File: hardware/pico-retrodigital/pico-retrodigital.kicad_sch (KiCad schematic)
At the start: 43 parts, among them J1 Conn_02x05_Top_Bottom, J2 HDMI_A, J4 Conn_01x02_Pin, J5 USB_C_Plug_USB2.0, SW1 SW_Push, U6 74LVC2G17, U7 RP2350B, U8 NCP1117-3.3_SOT223, Y1 ABM8-272-T3

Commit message: PCB fixes
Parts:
- removed J2: HDMI_A, Connector_Video:HDMI_A_Molex_208658-1001_Horizontal, symbol Connector:HDMI_A
- removed U6: 74LVC2G17, Package_TO_SOT_SMD:SOT-23-6, symbol pico-retrodigital:74LVC2G17_SINGLE
- added C16: 0.1u, Capacitor_SMD:C_0603_1608Metric, symbol Device:C
- added J3: Conn_01x14, Connector_FFC-FPC:TE_1-1734839-4_1x14-1MP_P0.5mm_Horizontal, symbol Connector_Generic:Conn_01x14
- added U1, U2: SN74LVC1G17DBVR, pico-retrodigital:SOT-23-5, symbol pico-retrodigital:SN74LVC1G17DBVR
- C14, C15: footprint RP2350_80QFN_minimal:C_0402_1005Metric_small_pads -> Capacitor_SMD:C_0402_1005Metric
- L1: footprint RP2350_80QFN_minimal:L_pol_2016 -> Inductor_SMD:L_0805_2012Metric
- R16, R17, R18: symbol Device:R_Small -> Device:R
- U3: renamed from U7; value RP2350B -> RP2354B; footprint rpi-lib-kicad-rp235x:QFN-80-1EP_10x10mm_P0.4mm_EP3.4x3.4mm_ThermalVias -> Package_DFN_QFN:QFN-80-1EP_10x10mm_P0.4mm_EP3.4x3.4mm_ThermalVias
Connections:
- net CTL_4 is gone; now on net CTL_2: U3.27 (GPIO26)
- net CTL_5 is gone; now on net CTL_3: U3.28 (GPIO27)
- net VBUS is gone; now on net 5V: C12.1, D3.1 (K), U8.3 (VI)
- net +3V3: now also C16.1, U1.5 (VCC)
- net 3V3: now also U2.5 (VCC)
- net AUD_CLK: now also U3.79 (GPIO2), U2.4 (Y)
- net AUD_DAT: now also U3.77 (GPIO0)
- net AUD_WS: now also U3.78 (GPIO1)
- net AUX_A: now also U3.8 (GPIO10)
- net AUX_B: now also U3.9 (GPIO11)
- net CEC_PICO: now also U3.22 (GPIO22), J3.6 (Pin_6)
- net CLK+: now also J3.8 (Pin_8)
- net CLK-: now also J3.7 (Pin_7)
- net CTL_0: now also U3.25 (GPIO24); no longer U3.22 (GPIO22)
- net CTL_1: now also U3.26 (GPIO25); no longer U3.23 (GPIO23)
- net CTL_2: no longer U3.25 (GPIO24)
- net CTL_3: no longer U3.26 (GPIO25)
- net D0+: now also J3.10 (Pin_10)
- net D0-: now also J3.9 (Pin_9)
- net D1+: now also J3.12 (Pin_12)
- net D1-: now also J3.11 (Pin_11)
- net D2+: now also J3.14 (Pin_14)
- net D2-: now also J3.13 (Pin_13)
- net GND: now also C16.2, J3.3 (Pin_3), U1.2 (GND), U2.2 (GND)
- net IN_AUD_CLK: now also U2.1 (A)
- net IN_PCLK: now also U1.1 (A)
- net PCLK: now also U1.4 (Y)
- net SCL: now also U3.21 (GPIO21), J3.5 (Pin_5)
- net SDA: now also U3.20 (GPIO20), J3.4 (Pin_4)
- net at C6.1, D2.1 (K): now also J3.1 (Pin_1)
- net at R2.2: now also J3.2 (Pin_2)
- no-connect marks 1 -> 21
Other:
- note added: "HDMI FFC"
- moved on the sheet: C6, D2, R1, R17, R18, R2

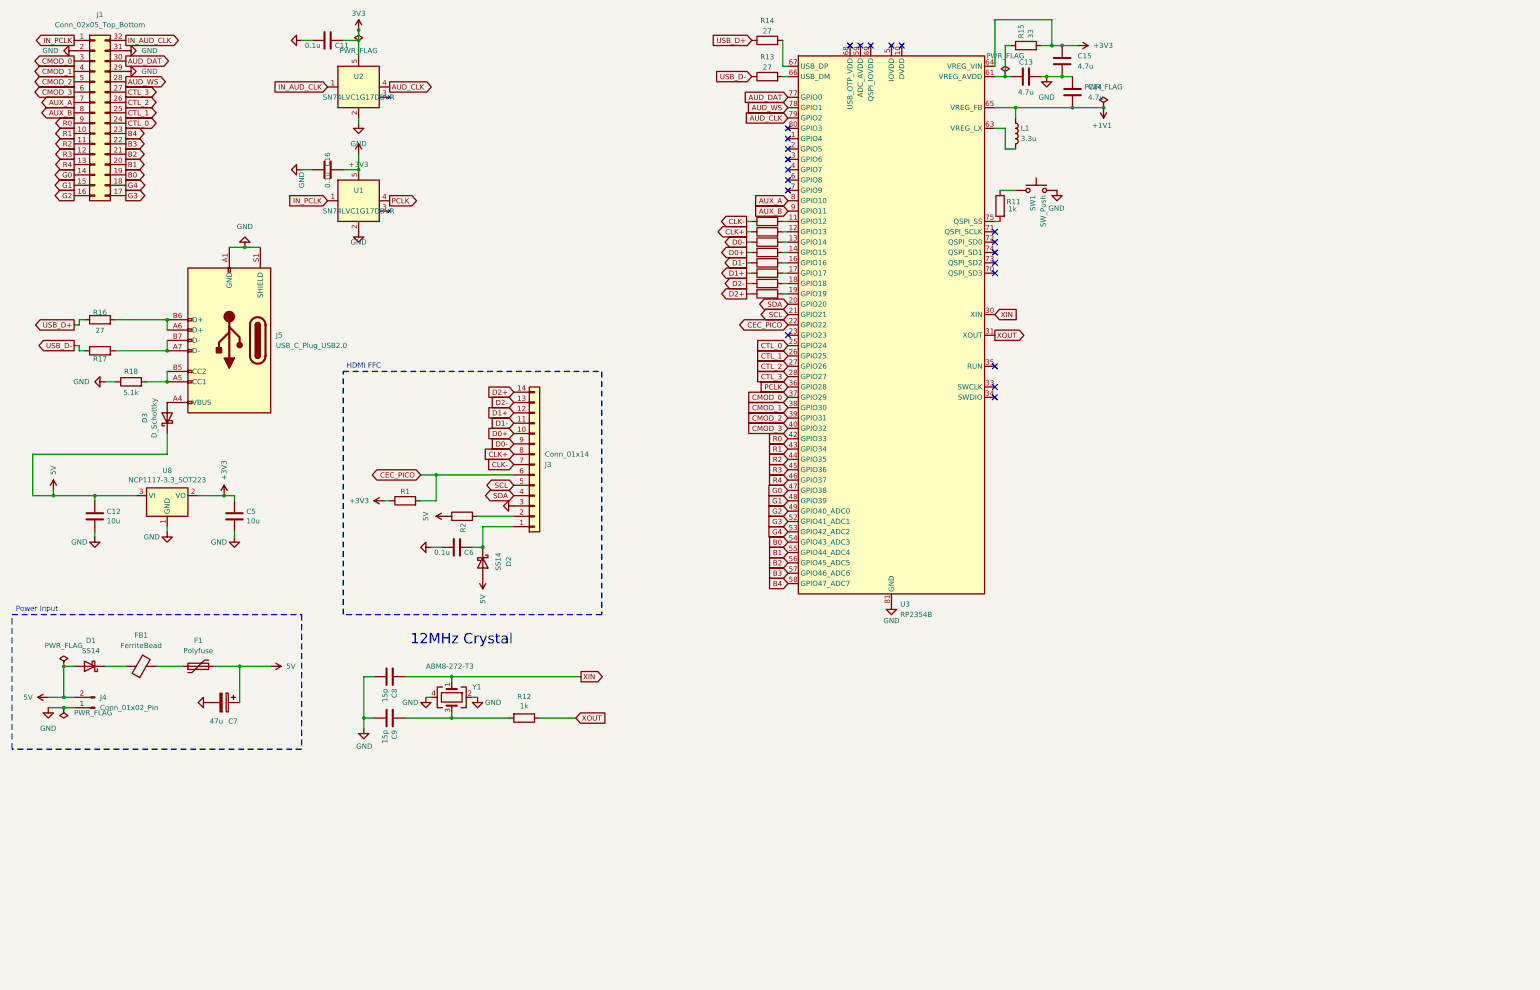
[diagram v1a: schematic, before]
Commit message: Square-shaped PCB
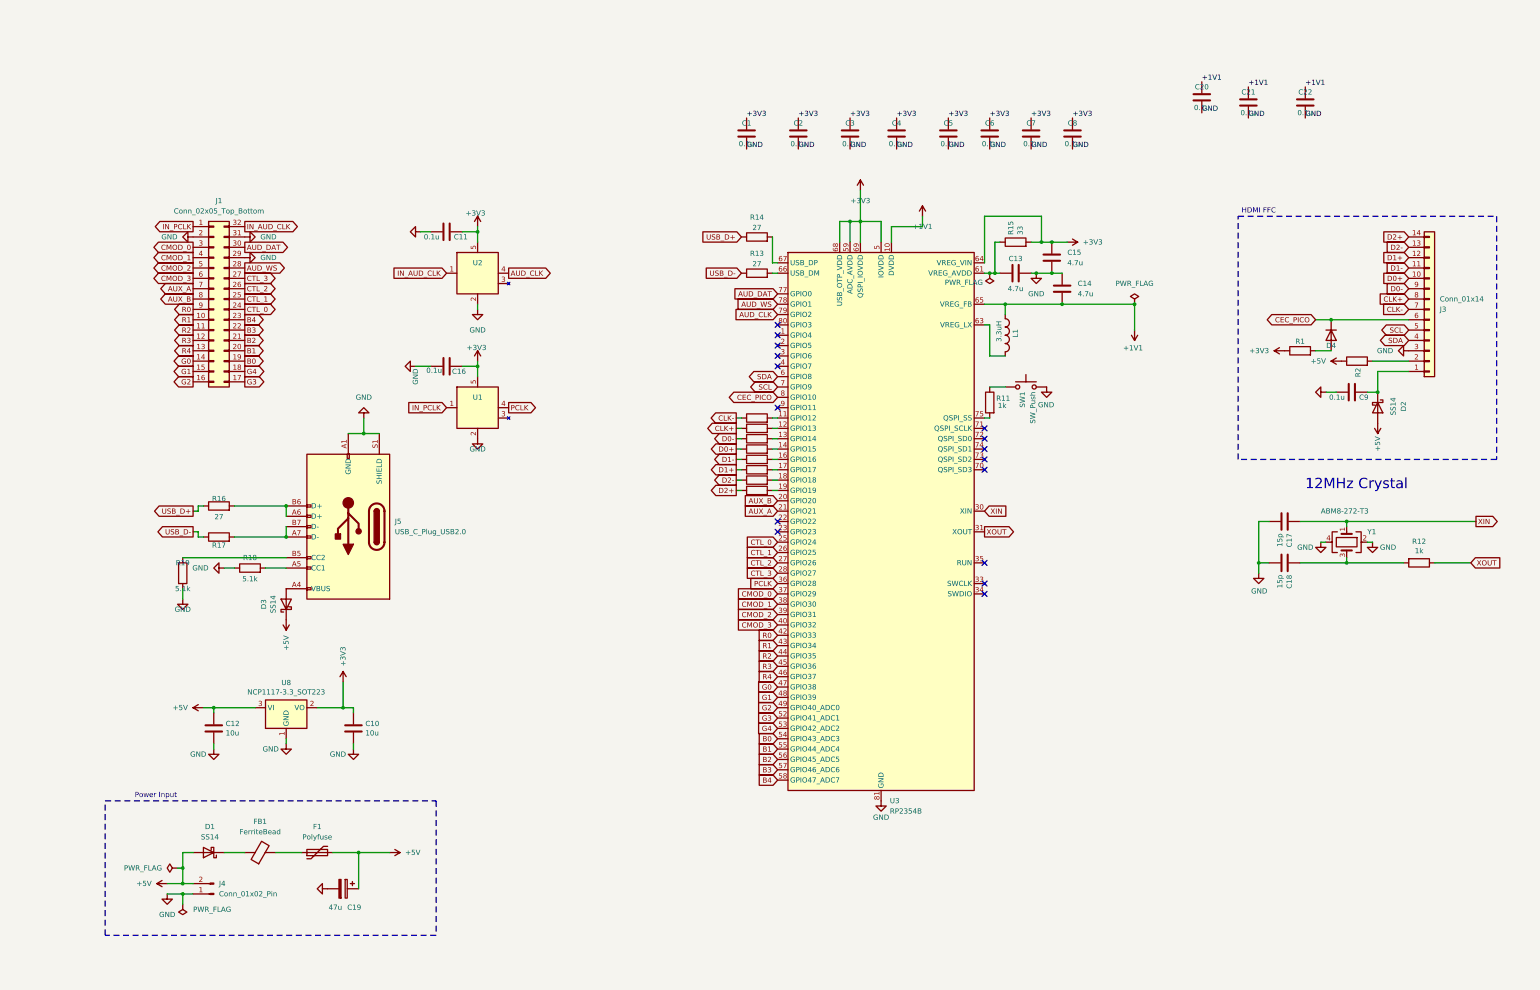
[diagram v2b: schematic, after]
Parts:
- removed L1: 3.3u, Inductor_SMD:L_0805_2012Metric, symbol Device:L
- added C1, C20, C21, C22, C3, C4, C5, C6, C7, C8: 0.1u, Capacitor_SMD:C_0402_1005Metric, symbol Device:C
- added C2: 0.1u, Capacitor_SMD:C_0603_1608Metric, symbol Device:C
- added D4: SS14, Diode_SMD:D_0603_1608Metric, symbol Diode:1N4148W
- added L1: (no value), pico-retrodigital:IND-SMD_L2.0-W1.6_AOTA-B201610S3R3-101-T, symbol ProPrj_RP2-easyedapro:AOTA-B201610S3R3-101-T
- added R19: 5.1k, Resistor_SMD:R_0603_1608Metric, symbol Device:R
- C11, C16: footprint Capacitor_SMD:C_0603_1608Metric -> Capacitor_SMD:C_0402_1005Metric
- C14: footprint Capacitor_SMD:C_0402_1005Metric -> Capacitor_SMD:C_0603_1608Metric
- C9: renamed from C6; footprint Capacitor_SMD:C_0603_1608Metric -> Capacitor_SMD:C_0402_1005Metric
- D3: value D_Schottky -> SS14; footprint Diode_SMD:D_SOD-123 -> Diode_SMD:D_0603_1608Metric
- R1: footprint Resistor_SMD:R_0603_1608Metric -> Resistor_SMD:R_0402_1005Metric
- U3: footprint Package_DFN_QFN:QFN-80-1EP_10x10mm_P0.4mm_EP3.4x3.4mm_ThermalVias -> rpi-lib-kicad-rp235x:QFN-80-1EP_10x10mm_P0.4mm_EP3.4x3.4mm_ThermalVias
- renumbered C5 to C10, C8 to C17, C9 to C18, C7 to C19
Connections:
- net 3V3 is gone; now on net +3V3: C11.1, U2.5 (VCC)
- net +1V1: now also U3.10 (DVDD), U3.32 (DVDD), U3.51 (DVDD), C20.1, C21.1, C22.1, L1.1
- net +3V3: now also U3.15 (IOVDD), U3.24 (IOVDD), U3.29 (IOVDD), U3.41 (IOVDD), U3.5 (IOVDD), U3.50 (IOVDD), U3.59 (ADC_AVDD), U3.60 (IOVDD), U3.68 (USB_OTP_VDD), U3.69 (QSPI_IOVDD), U3.76 (IOVDD), C1.1, C2.1, C3.1, C4.1, C5.1, C6.1, C7.1, C8.1
- net AUX_A: now also U3.21 (GPIO21); no longer U3.8 (GPIO10)
- net AUX_B: now also U3.20 (GPIO20); no longer U3.9 (GPIO11)
- net CEC_PICO: now also U3.8 (GPIO10), D4.1 (K); no longer R1.2, U3.22 (GPIO22)
- net GND: now also C1.2, C2.2, C20.2, C21.2, C22.2, C3.2, C4.2, C5.2, C6.2, C7.2, C8.2, R19.2
- net SCL: now also U3.7 (GPIO9); no longer U3.21 (GPIO21)
- net SDA: now also U3.6 (GPIO8); no longer U3.20 (GPIO20)
- net at U3.63 (VREG_LX): now also L1.2
- net at J5.A5 (CC1), R18.2: no longer J5.B5 (CC2)
- net 5V renamed +5V
- new net: J5.B5 (CC2), R19.1
- new net: D4.2 (A), R1.2
- no-connect marks 21 -> 16
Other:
- moved on the sheet: C10, C11, C12, C13, C14, C15, C16, C17, C18, C19, C9, D1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

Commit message: Add 3V3 LDO regulator, reset/boot buttons, and pad default tweaks
- Add ME6217C33M5G LDO symbol and integrate into schematic
- Add RES1 (reset) and BOOT1 (boot) push buttons
- Update default pad size in board setup
- Ignore kicad-jlcpcb-tools plugin local state (jlcpcb/)
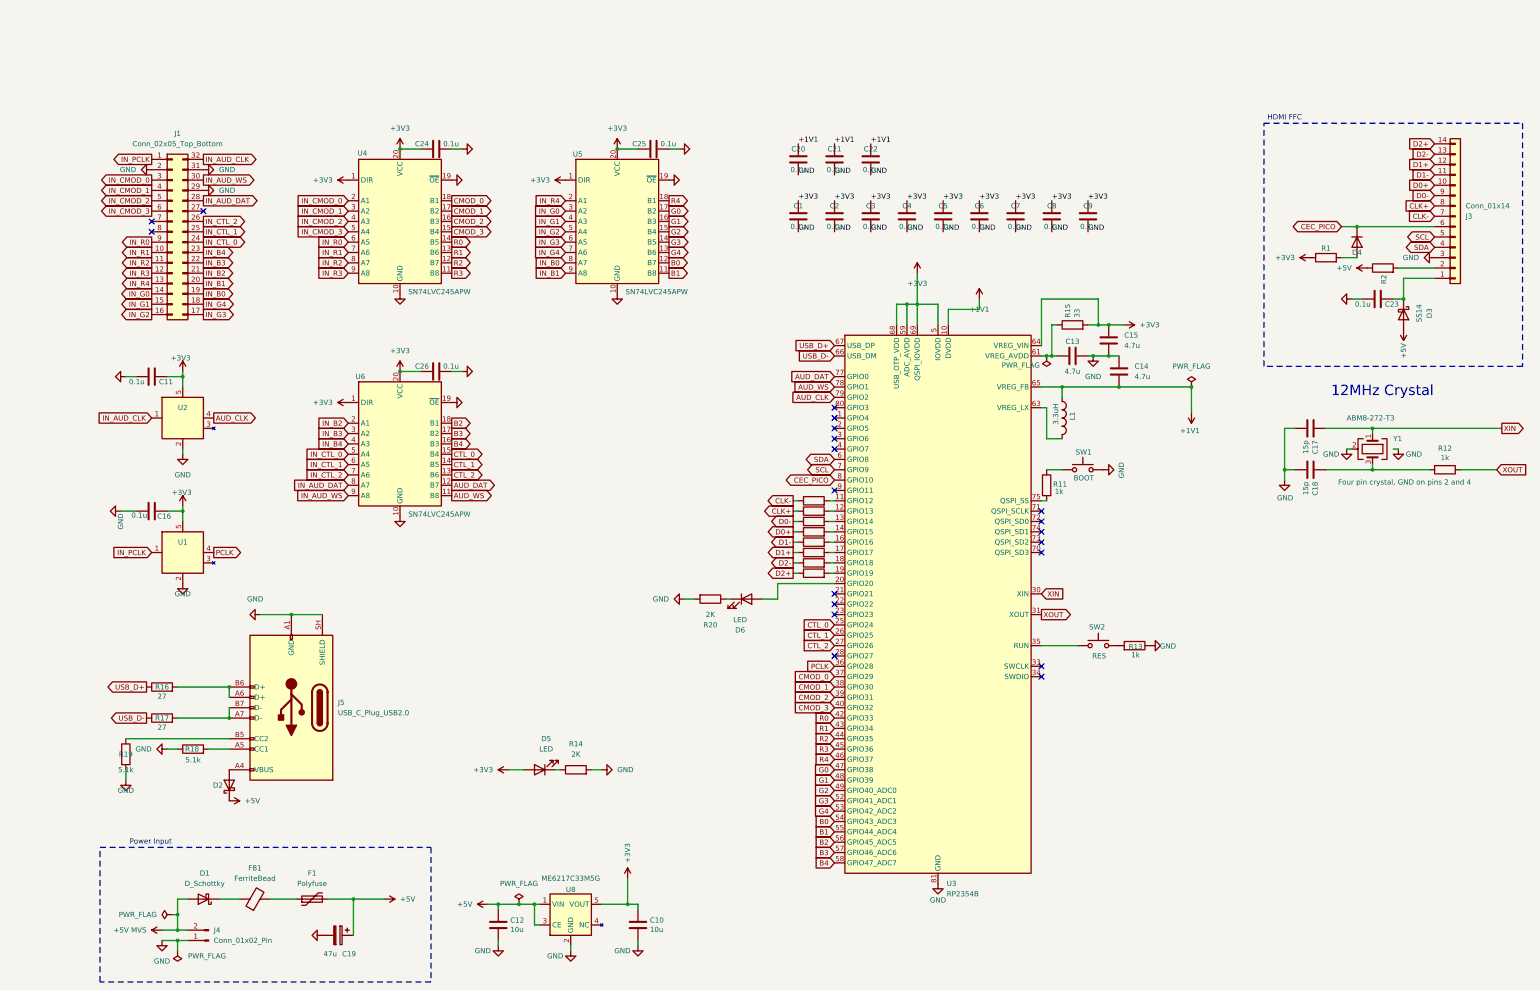
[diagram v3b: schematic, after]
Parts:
- added C24, C25, C26, C9: 0.1u, Capacitor_SMD:C_0402_1005Metric, symbol Device:C
- added D5, D6: LED, LED_SMD:LED_0603_1608Metric, symbol Device:LED
- added R20: 2K, Resistor_SMD:R_0402_1005Metric, symbol Device:R
- added SW2: RES, Button_Switch_SMD:SW_Push_1P1T_NO_Vertical_Wuerth_434133025816, symbol Switch:SW_Push
- added U4, U5, U6: SN74LVC245APW, Package_SO:TSSOP-20_4.4x6.5mm_P0.65mm, symbol Logic_LevelTranslator:SN74LVC245APW
- D1: value SS14 -> D_Schottky; footprint Diode_SMD:D_0603_1608Metric -> Diode_SMD:D_SOD-123
- D2: renamed from D3; value SS14 -> D_Schottky; footprint Diode_SMD:D_0603_1608Metric -> Diode_SMD:D_SOD-123
- J4: footprint Connector_PinHeader_2.54mm:PinHeader_1x02_P2.54mm_Vertical -> Connector_JST:JST_XA_B02B-XASK-1_1x02_P2.50mm_Vertical
- J5: footprint pico-retrodigital:USB_C_Receptacle_Jing_918-418K2023S40001 -> Connector_USB:USB_C_Receptacle_GCT_USB4105-xx-A_16P_TopMnt_Horizontal
- R13: value 27 -> 1k
- R14: value 27 -> 2K
- SW1: value SW_Push -> BOOT
- U8: value NCP1117-3.3_SOT223 -> ME6217C33M5G; footprint Package_TO_SOT_SMD:SOT-223-3_TabPin2 -> Package_TO_SOT_SMD:SOT-23-5; symbol Regulator_Linear:NCP1117-3.3_SOT223 -> pico-retrodigital:ME6217C33M5G
- renumbered C9 to C23, D2 to D3
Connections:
- net +3V3: now also U8.5 (VOUT), C24.1, C25.1, C26.1, C9.1, D5.2 (A), U4.1 (DIR), U4.20 (VCC), U5.1 (DIR), U5.20 (VCC), U6.1 (DIR), U6.20 (VCC); no longer U8.2 (VO)
- net +5V: now also U8.1 (VIN); no longer D1.2 (A), J4.2 (Pin_2)
- net AUD_DAT: now also U6.12 (B7); no longer J1.30 (Pin_30)
- net AUD_WS: now also U6.11 (B8); no longer J1.28 (Pin_28)
- net B0: now also U5.12 (B7); no longer J1.19 (Pin_19)
- net B1: now also U5.11 (B8); no longer J1.20 (Pin_20)
- net B2: now also U6.18 (B1); no longer J1.21 (Pin_21)
- net B3: now also U6.17 (B2); no longer J1.22 (Pin_22)
- net B4: now also U6.16 (B3); no longer J1.23 (Pin_23)
- net CMOD_0: now also U4.18 (B1); no longer J1.3 (Pin_3)
- net CMOD_1: now also U4.17 (B2); no longer J1.4 (Pin_4)
- net CMOD_2: now also U4.16 (B3); no longer J1.5 (Pin_5)
- net CMOD_3: now also U4.15 (B4); no longer J1.6 (Pin_6)
- net CTL_0: now also U6.15 (B4); no longer J1.24 (Pin_24)
- net CTL_1: now also U6.14 (B5); no longer J1.25 (Pin_25)
- net CTL_2: now also U6.13 (B6); no longer J1.26 (Pin_26)
- net G0: now also U5.17 (B2); no longer J1.14 (Pin_14)
- net G1: now also U5.16 (B3); no longer J1.15 (Pin_15)
- net G2: now also U5.15 (B4); no longer J1.16 (Pin_16)
- net G3: now also U5.14 (B5); no longer J1.17 (Pin_17)
- net G4: now also U5.13 (B6); no longer J1.18 (Pin_18)
- net GND: now also J5.SH (SHIELD), R13.1, R14.2, U8.2 (GND), C24.2, C25.2, C26.2, C9.2, R20.2, U4.10 (GND), U4.19 (~{OE}), U5.10 (GND), U5.19 (~{OE}), U6.10 (GND), U6.19 (~{OE}); no longer J5.S1 (SHIELD), U8.1 (GND)
- net R0: now also U4.14 (B5); no longer J1.9 (Pin_9)
- net R1: now also U4.13 (B6); no longer J1.10 (Pin_10)
- net R2: now also U4.12 (B7); no longer J1.11 (Pin_11)
- net R3: now also U4.11 (B8); no longer J1.12 (Pin_12)
- net R4: now also U5.18 (B1); no longer J1.13 (Pin_13)
- net USB_D+: now also U3.67 (USB_DP); no longer R14.1
- net USB_D-: now also U3.66 (USB_DM); no longer R13.1
- net at R13.2: now also SW2.1; no longer U3.66 (USB_DM)
- net at U3.35 (RUN): now also SW2.2
- net AUX_A: no longer names the net of J1.7 (Pin_7)
- net AUX_A: no longer U3.21 (GPIO21)
- net AUX_B: no longer names the net of J1.8 (Pin_8)
- net AUX_B: no longer U3.20 (GPIO20)
- net CTL_3: no longer names the net of J1.27 (Pin_27)
- net CTL_3: no longer U3.28 (GPIO27)
- new net: D5.1 (K), R14.1
- new net: D6.1 (K), R20.1
- new net: D6.2 (A), U3.20 (GPIO20)
- new net +5V MVS: D1.2 (A), J4.2 (Pin_2)
- new net IN_AUD_DAT: J1.28 (Pin_28), U6.8 (A7)
- new net IN_AUD_WS: J1.30 (Pin_30), U6.9 (A8)
- new net IN_B0: J1.19 (Pin_19), U5.8 (A7)
- new net IN_B1: J1.20 (Pin_20), U5.9 (A8)
- new net IN_B2: J1.21 (Pin_21), U6.2 (A1)
- new net IN_B3: J1.22 (Pin_22), U6.3 (A2)
- new net IN_B4: J1.23 (Pin_23), U6.4 (A3)
- new net IN_CMOD_0: J1.3 (Pin_3), U4.2 (A1)
- new net IN_CMOD_1: J1.4 (Pin_4), U4.3 (A2)
- new net IN_CMOD_2: J1.5 (Pin_5), U4.4 (A3)
- new net IN_CMOD_3: J1.6 (Pin_6), U4.5 (A4)
- new net IN_CTL_0: J1.24 (Pin_24), U6.5 (A4)
- new net IN_CTL_1: J1.25 (Pin_25), U6.6 (A5)
- new net IN_CTL_2: J1.26 (Pin_26), U6.7 (A6)
- new net IN_G0: J1.14 (Pin_14), U5.3 (A2)
- new net IN_G1: J1.15 (Pin_15), U5.4 (A3)
- new net IN_G2: J1.16 (Pin_16), U5.5 (A4)
- new net IN_G3: J1.17 (Pin_17), U5.6 (A5)
- new net IN_G4: J1.18 (Pin_18), U5.7 (A6)
- new net IN_R0: J1.9 (Pin_9), U4.6 (A5)
- new net IN_R1: J1.10 (Pin_10), U4.7 (A6)
- new net IN_R2: J1.11 (Pin_11), U4.8 (A7)
- new net IN_R3: J1.12 (Pin_12), U4.9 (A8)
- new net IN_R4: J1.13 (Pin_13), U5.2 (A1)
- no-connect marks 16 -> 20
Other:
- moved on the sheet: C1, C10, C11, C12, C13, C14, C15, C16, C17, C18, C19, C2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

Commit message: Update PCB
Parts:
- L1: symbol ProPrj_RP2-easyedapro:AOTA-B201610S3R3-101-T -> pico-retrodigital:AOTA-B201610S3R3-101-T
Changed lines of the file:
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@@
 	(wire
 		(pts
-			(xy 353.06 121.92) (xy 354.33 121.92)
-		)
-		(stroke
-			(width 0)
-			(type default)
-		)
-	)
-	(wire
-		(pts
 			(xy 283.21 99.06) (xy 285.75 99.06)
 		)
@@
 	)
 	(symbol
-		(lib_id "ProPrj_RP2-easyedapro:AOTA-B201610S3R3-101-T")
+		(lib_id "pico-retrodigital:AOTA-B201610S3R3-101-T")
 		(at 271.78 114.3 270)
 		(unit 1)
@@
 					(unit 1)
 				)
-			)
-		)
-	)
-	(symbol
-		(lib_id "power:GND")
-		(at 354.33 121.92 0)
-		(unit 1)
-		(body_style 1)
-		(exclude_from_sim no)
-		(in_bom yes)
-		(on_board yes)
-		(in_pos_files yes)
-		(dnp no)
-		(property "Reference" "#PWR031"
-			(at 354.33 128.27 0)
-			(hide yes)
-			(show_name no)
-			(do_not_autoplace no)
-			(effects
-				(font
-					(size 1.27 1.27)
-				)
-			)
-		)
-		(property "Value" "GND"
-			(at 358.14 123.19 0)
-			(show_name no)
-			(do_not_autoplace no)
-			(effects
-				(font
-					(size 1.27 1.27)
-				)
-			)
-		)
-		(property "Footprint" ""
-			(at 354.33 121.92 0)
-			(hide yes)
-			(show_name no)
-			(do_not_autoplace no)
-			(effects
-				(font
-					(size 1.27 1.27)
-				)
-			)
-		)
-		(property "Datasheet" ""
-			(at 354.33 121.92 0)
-			(hide yes)
-			(show_name no)
-			(do_not_autoplace no)
-			(effects
-				(font
-					(size 1.27 1.27)
-				)
-			)
-		)
-		(property "Description" ""
-			(at 354.33 121.92 0)
-			(show_name no)
-			(do_not_autoplace no)
-			(effects
-				(font
-					(size 1.27 1.27)
-				)
-			)
-		)
-		(pin "1"
-		)
-		(instances
-			(project "pico-retrodigital"
-				(path "/520ac6ec-80ea-49af-90b4-82d4dc9702db"
-					(reference "#PWR031")
-					(unit 1)
-				)

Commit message: Add JLCPCB part numbers
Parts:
- SW1, SW2: JLCPCB (none) -> C92589
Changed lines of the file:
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@@
 			)
 		)
+		(property "JLCPCB" "C92589"
+			(at 280.67 170.18 0)
+			(hide yes)
+			(show_name no)
+			(do_not_autoplace no)
+			(effects
+				(font
+					(size 1.27 1.27)
+				)
+			)
+		)
 		(pin "1"
 		)
@@
 			(show_name no)
 			(do_not_autoplace no)
+			(effects
+				(font
+					(size 1.27 1.27)
+				)
+			)
+		)
+		(property "JLCPCB" "C92589"
+			(at 276.86 127 0)
+			(hide yes)
+			(show_name no)
+			(do_not_autoplace no)
